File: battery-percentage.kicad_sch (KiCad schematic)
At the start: 12 parts, among them J1 Conn_01x06, SW1 SW_Push, U1 WeMos_D1_mini, U2 LM7805_TO220

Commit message: Updated Schematic
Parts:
- removed D1: LED, LED_THT:LED_D1.8mm_W3.3mm_H2.4mm, symbol Device:LED
- removed R4: 1k, Resistor_THT:R_Axial_DIN0204_L3.6mm_D1.6mm_P5.08mm_Horizontal, symbol Device:R
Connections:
- net +12V: now also C3.2
- net GND: now also C1.2, C3.1; no longer C3.2
- net D1: now reaches U1.14 (SCL/D1)
- net D1: now also J1.2 (Pin_2)
- net D4: no longer names the net of U1.11 (D4)
- net D4: no longer J1.2 (Pin_2)
- no-connect marks 0 -> 9
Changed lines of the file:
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@@
   (junction (at 100.584 80.645) (diameter 0) (color 0 0 0 0)
   )
+  (junction (at 100.584 93.345) (diameter 0) (color 0 0 0 0)
+  )
   (junction (at 105.156 37.211) (diameter 0) (color 0 0 0 0)
   )
@@
   (junction (at 105.156 34.671) (diameter 0) (color 0 0 0 0)
   )
+  (no_connect (at 46.736 59.817))
+  (no_connect (at 46.736 64.897))
+  (no_connect (at 46.736 54.737))
+  (no_connect (at 46.736 44.577))
+  (no_connect (at 26.416 44.577))
+  (no_connect (at 46.736 49.657))
+  (no_connect (at 46.736 62.357))
+  (no_connect (at 46.736 57.277))
+  (no_connect (at 39.116 34.417))
   (wire (pts (xy 112.268 93.345) (xy 112.268 94.615))
     (stroke (width 0) (type default))
@@
     (stroke (width 0) (type default))
   )
-  (wire (pts (xy 110.109 93.345) (xy 112.268 93.345))
-    (stroke (width 0) (type default))
-  )
   (wire (pts (xy 123.952 80.645) (xy 123.952 78.359))
     (stroke (width 0) (type default))
   )
+  (wire (pts (xy 100.584 93.345) (xy 112.268 93.345))
+    (stroke (width 0) (type default))
+  )
   (wire (pts (xy 105.283 37.211) (xy 105.156 37.211))
     (stroke (width 0) (type default))
   )
+  (wire (pts (xy 94.996 93.345) (xy 94.996 90.805))
+    (stroke (width 0) (type default))
+  )
   (wire (pts (xy 123.952 83.185) (xy 123.952 80.645))
     (stroke (width 0) (type default))
   )
-  (wire (pts (xy 155.448 46.355) (xy 155.448 48.895))
-    (stroke (width 0) (type default))
-  )
   (wire (pts (xy 100.584 83.185) (xy 100.584 80.645))
     (stroke (width 0) (type default))
@@
     (stroke (width 0) (type default))
   )
-  (wire (pts (xy 49.276 54.737) (xy 46.736 54.737))
-    (stroke (width 0) (type default))
-  )
   (wire (pts (xy 71.247 33.528) (xy 71.247 35.814))
     (stroke (width 0) (type default))
@@
     (stroke (width 0) (type default))
   )
-  (wire (pts (xy 100.584 93.345) (xy 102.489 93.345))
+  (wire (pts (xy 94.996 93.345) (xy 100.584 93.345))
     (stroke (width 0) (type default))
   )
@@
     (stroke (width 0) (type default))
   )
-  (wire (pts (xy 155.448 36.195) (xy 155.448 38.735))
-    (stroke (width 0) (type default))
-  )
   (wire (pts (xy 112.268 88.265) (xy 112.268 93.345))
     (stroke (width 0) (type default))
   )
-  (wire (pts (xy 155.448 56.515) (xy 155.448 59.055))
-    (stroke (width 0) (type default))
-  )
   (wire (pts (xy 102.743 47.371) (xy 102.743 44.831))
     (stroke (width 0) (type default))
@@
     (stroke (width 0) (type default))
   )
+  (wire (pts (xy 49.276 47.117) (xy 46.736 47.117))
+    (stroke (width 0) (type default))
+  )
   (wire (pts (xy 105.283 47.371) (xy 105.156 47.371))
     (stroke (width 0) (type default))
@@
     (stroke (width 0) (type default))
   )
+  (wire (pts (xy 94.996 83.185) (xy 94.996 80.645))
+    (stroke (width 0) (type default))
+  )
   (wire (pts (xy 105.156 39.751) (xy 102.743 39.751))
     (stroke (width 0) (type default))
   )
   (wire (pts (xy 105.156 34.671) (xy 102.743 34.671))
+    (stroke (width 0) (type default))
+  )
+  (wire (pts (xy 94.996 80.645) (xy 100.584 80.645))
     (stroke (width 0) (type default))
   )
@@
     (effects (font (size 1.27 1.27)) (justify right bottom))
   )
-  (label "D4" (at 49.276 54.737 0) (fields_autoplaced)
-    (effects (font (size 1.27 1.27)) (justify left bottom))
-  )
   (label "FLASH" (at 134.874 43.434 90) (fields_autoplaced)
     (effects (font (size 1.27 1.27)) (justify left bottom))
@@
     (effects (font (size 1.27 1.27)) (justify right bottom))
   )
+  (label "D1" (at 49.276 47.117 0) (fields_autoplaced)
+    (effects (font (size 1.27 1.27)) (justify left bottom))
+  )
   (label "A0" (at 46.736 42.037 0) (fields_autoplaced)
     (effects (font (size 1.27 1.27)) (justify left bottom))
   )
-  (label "D4" (at 102.743 37.211 180) (fields_autoplaced)
+  (label "D1" (at 102.743 37.211 180) (fields_autoplaced)
     (effects (font (size 1.27 1.27)) (justify right bottom))
   )
@@
     )
   )
-  (symbol (lib_id "Device:LED") (at 155.448 42.545 90) (unit 1)
-    (in_bom yes) (on_board yes) (dnp no) (fields_autoplaced)
-    (property "Reference" "D1" (at 158.369 43.4975 90)
-      (effects (font (size 1.27 1.27)) (justify right))
-    )
-    (property "Value" "LED" (at 158.369 46.0375 90)
-      (effects (font (size 1.27 1.27)) (justify right))
-    )
-    (property "Footprint" "LED_THT:LED_D1.8mm_W3.3mm_H2.4mm" (at 155.448 42.545 0)
-      (effects (font (size 1.27 1.27)) hide)
-    )
-    (property "Datasheet" "~" (at 155.448 42.545 0)
-      (effects (font (size 1.27 1.27)) hide)
-    )
-    (pin "1")
-    (pin "2")
-    (instances
-      (project "battery-percentage"
-        (path "/f79966b4-4927-4ec7-886d-17305cb22602"
-          (reference "D1") (unit 1)
-        )
-      )
-    )
-  )
   (symbol (lib_id "power:GND") (at 134.874 58.674 0) (unit 1)
     (in_bom yes) (on_board yes) (dnp no) (fields_autoplaced)
@@
         (path "/f79966b4-4927-4ec7-886d-17305cb22602"
           (reference "#PWR08") (unit 1)
-        )
-      )
-    )
-  )
-  (symbol (lib_id "Device:C") (at 106.299 93.345 90) (unit 1)
-    (in_bom yes) (on_board yes) (dnp no)
-    (property "Reference" "C3" (at 104.14 94.742 90)
-      (effects (font (size 1.27 1.27)) (justify left))
-    )
-    (property "Value" "0.1uF" (at 107.188 96.647 90)
-      (effects (font (size 1.27 1.27)) (justify left))
-    )
-    (property "Footprint" "Capacitor_THT:CP_Radial_D4.0mm_P1.50mm" (at 110.109 92.3798 0)
-      (effects (font (size 1.27 1.27)) hide)
-    )
-    (property "Datasheet" "~" (at 106.299 93.345 0)
-      (effects (font (size 1.27 1.27)) hide)
-    )
-    (pin "1")
-    (pin "2")
-    (instances
-      (project "battery-percentage"
-        (path "/f79966b4-4927-4ec7-886d-17305cb22602"
-          (reference "C3") (unit 1)
         )
       )
@@
     )
   )
-  (symbol (lib_id "power:GND") (at 155.448 59.055 0) (unit 1)
-    (in_bom yes) (on_board yes) (dnp no) (fields_autoplaced)
-    (property "Reference" "#PWR012" (at 155.448 65.405 0)
-      (effects (font (size 1.27 1.27)) hide)
-    )
-    (property "Value" "GND" (at 155.448 63.754 0)
-      (effects (font (size 1.27 1.27)))
-    )
-    (property "Footprint" "" (at 155.448 59.055 0)
-      (effects (font (size 1.27 1.27)) hide)
-    )
-    (property "Datasheet" "" (at 155.448 59.055 0)
-      (effects (font (size 1.27 1.27)) hide)
-    )
-    (pin "1")
-    (instances
-      (project "battery-percentage"
-        (path "/f79966b4-4927-4ec7-886d-17305cb22602"
-          (reference "#PWR012") (unit 1)
-        )
-      )
-    )
-  )
   (symbol (lib_id "power:+5V") (at 123.952 78.359 0) (unit 1)
     (in_bom yes) (on_board yes) (dnp no) (fields_autoplaced)
@@
   (symbol (lib_id "Device:C") (at 100.584 86.995 0) (unit 1)
     (in_bom yes) (on_board yes) (dnp no)
-    (property "Reference" "C1" (at 93.472 85.979 0)
-      (effects (font (size 1.27 1.27)) (justify left))
-    )
-    (property "Value" "0.2uF" (at 91.821 87.884 0)
+    (property "Reference" "C1" (at 104.902 86.106 0)
+      (effects (font (size 1.27 1.27)) (justify left))
+    )
+    (property "Value" "0.2uF" (at 103.251 88.011 0)
       (effects (font (size 1.27 1.27)) (justify left))
     )
@@
     )
   )
-  (symbol (lib_id "power:+5V") (at 155.448 36.195 0) (unit 1)
-    (in_bom yes) (on_board yes) (dnp no) (fields_autoplaced)
-    (property "Reference" "#PWR011" (at 155.448 40.005 0)
-      (effects (font (size 1.27 1.27)) hide)
-    )
-    (property "Value" "+5V" (at 155.448 32.639 0)
-      (effects (font (size 1.27 1.27)))
-    )
-    (property "Footprint" "" (at 155.448 36.195 0)
-      (effects (font (size 1.27 1.27)) hide)
-    )
-    (property "Datasheet" "" (at 155.448 36.195 0)
-      (effects (font (size 1.27 1.27)) hide)
-    )
-    (pin "1")
-    (instances
-      (project "battery-percentage"
-        (path "/f79966b4-4927-4ec7-886d-17305cb22602"
-          (reference "#PWR011") (unit 1)
-        )
-      )
-    )
-  )
   (symbol (lib_id "Device:R") (at 71.247 39.624 0) (unit 1)
     (in_bom yes) (on_board yes) (dnp no) (fields_autoplaced)
@@
         (path "/f79966b4-4927-4ec7-886d-17305cb22602"
           (reference "#PWR03") (unit 1)
-        )
-      )
-    )
-  )
-  (symbol (lib_id "Device:R") (at 155.448 52.705 0) (unit 1)
-    (in_bom yes) (on_board yes) (dnp no) (fields_autoplaced)
-    (property "Reference" "R4" (at 158.369 52.07 0)
-      (effects (font (size 1.27 1.27)) (justify left))
-    )
-    (property "Value" "1k" (at 158.369 54.61 0)
-      (effects (font (size 1.27 1.27)) (justify left))
-    )
-    (property "Footprint" "Resistor_THT:R_Axial_DIN0204_L3.6mm_D1.6mm_P5.08mm_Horizontal" (at 153.67 52.705 90)
-      (effects (font (size 1.27 1.27)) hide)
-    )
-    (property "Datasheet" "~" (at 155.448 52.705 0)
-      (effects (font (size 1.27 1.27)) hide)
-    )
-    (pin "1")
-    (pin "2")
-    (instances
-      (project "battery-percentage"
-        (path "/f79966b4-4927-4ec7-886d-17305cb22602"
-          (reference "R4") (unit 1)
         )
       )
@@
         )
       )
+    )
+  )
+  (symbol (lib_id "Device:C") (at 94.996 86.995 180) (unit 1)
+    (in_bom yes) (on_board yes) (dnp no)
+    (property "Reference" "C3" (at 91.313 88.265 0)
+      (effects (font (size 1.27 1.27)) (justify left))
+    )
+    (property "Value" "0.1uF" (at 92.075 86.233 0)
+      (effects (font (size 1.27 1.27)) (justify left))
+    )
+    (property "Footprint" "Capacitor_THT:CP_Radial_D4.0mm_P1.50mm" (at 94.0308 83.185 0)
+      (effects (font (size 1.27 1.27)) hide)
+    )
+    (property "Datasheet" "~" (at 94.996 86.995 0)
+      (effects (font (size 1.27 1.27)) hide)
+    )
+    (pin "1")
+    (pin "2")
+    (instances
+      (project "battery-percentage"
+        (path "/f79966b4-4927-4ec7-886d-17305cb22602"
+          (reference "C3") (unit 1)
+        )
+      )

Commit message: Updated Schematic
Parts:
- removed J1: Conn_01x06, Connector_PinHeader_2.00mm:PinHeader_1x06_P2.00mm_Horizontal, symbol Connector_Generic:Conn_01x06
- added J2: Conn_01x07, symbol Connector_Generic:Conn_01x07
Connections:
- net +12V: now also J2.1 (Pin_1)
- net +5V: now also J2.5 (Pin_5)
- net D1: now also J2.2 (Pin_2)
- net GND: now also J2.6 (Pin_6), J2.7 (Pin_7)
- net RX: now also J2.3 (Pin_3)
- net TX: now also J2.4 (Pin_4)

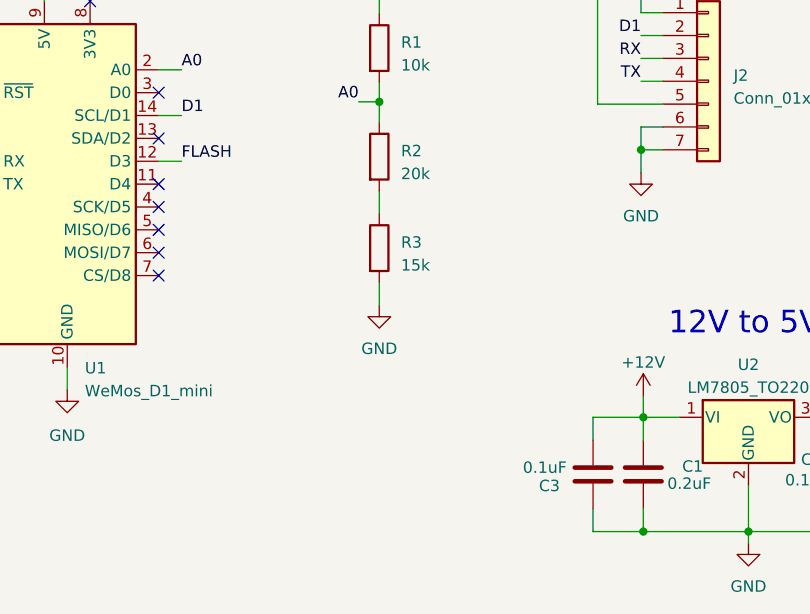
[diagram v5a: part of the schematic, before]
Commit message: Updated Potential Divider Values
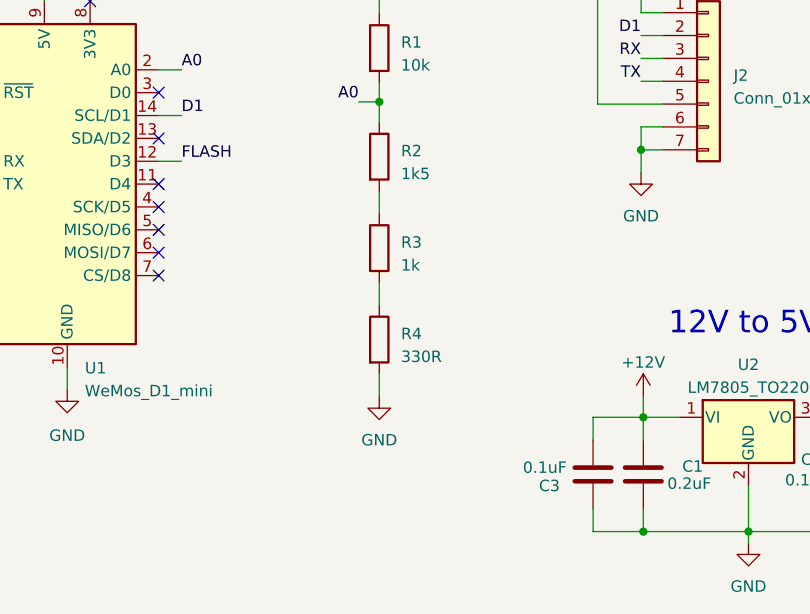
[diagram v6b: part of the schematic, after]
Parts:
- added R4: 330R, Resistor_THT:R_Axial_DIN0204_L3.6mm_D1.6mm_P5.08mm_Horizontal, symbol Device:R
- R2: value 20k -> 1k5
- R3: value 15k -> 1k
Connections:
- net GND: now also R4.2; no longer R3.2
- new net: R3.2, R4.1
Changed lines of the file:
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@@
-    (stroke (width 0) (type default))
-  )
-  (wire (pts (xy 71.247 68.199) (xy 71.247 65.659))
     (stroke (width 0) (type default))
   )
@@
     (stroke (width 0) (type default))
   )
+  (wire (pts (xy 71.247 65.659) (xy 71.247 68.199))
+    (stroke (width 0) (type default))
+  )
   (wire (pts (xy 100.33 35.687) (xy 102.743 35.687))
     (stroke (width 0) (type default))
@@
   )
   (wire (pts (xy 49.276 42.037) (xy 46.736 42.037))
+    (stroke (width 0) (type default))
+  )
+  (wire (pts (xy 71.247 78.359) (xy 71.247 75.819))
     (stroke (width 0) (type default))
   )
@@
     )
   )
-  (symbol (lib_id "power:GND") (at 71.247 68.199 0) (unit 1)
-    (in_bom yes) (on_board yes) (dnp no) (fields_autoplaced)
-    (property "Reference" "#PWR05" (at 71.247 74.549 0)
-      (effects (font (size 1.27 1.27)) hide)
-    )
-    (property "Value" "GND" (at 71.247 73.025 0)
-      (effects (font (size 1.27 1.27)))
-    )
-    (property "Footprint" "" (at 71.247 68.199 0)
-      (effects (font (size 1.27 1.27)) hide)
-    )
-    (property "Datasheet" "" (at 71.247 68.199 0)
-      (effects (font (size 1.27 1.27)) hide)
-    )
-    (pin "1")
-    (instances
-      (project "battery-percentage"
-        (path "/f79966b4-4927-4ec7-886d-17305cb22602"
-          (reference "#PWR05") (unit 1)
-        )
-      )
-    )
-  )
   (symbol (lib_id "Device:R") (at 71.247 51.689 0) (unit 1)
     (in_bom yes) (on_board yes) (dnp no) (fields_autoplaced)
@@
       (effects (font (size 1.27 1.27)) (justify left))
     )
-    (property "Value" "20k" (at 73.66 53.594 0)
+    (property "Value" "1k5" (at 73.66 53.594 0)
       (effects (font (size 1.27 1.27)) (justify left))
     )
@@
       (effects (font (size 1.27 1.27)) (justify left))
     )
-    (property "Value" "15k" (at 73.66 63.754 0)
+    (property "Value" "1k" (at 73.66 63.754 0)
       (effects (font (size 1.27 1.27)) (justify left))
     )
@@
     )
   )
+  (symbol (lib_id "power:GND") (at 71.247 78.359 0) (unit 1)
+    (in_bom yes) (on_board yes) (dnp no) (fields_autoplaced)
+    (property "Reference" "#PWR05" (at 71.247 84.709 0)
+      (effects (font (size 1.27 1.27)) hide)
+    )
+    (property "Value" "GND" (at 71.247 83.185 0)
+      (effects (font (size 1.27 1.27)))
+    )
+    (property "Footprint" "" (at 71.247 78.359 0)
+      (effects (font (size 1.27 1.27)) hide)
+    )
+    (property "Datasheet" "" (at 71.247 78.359 0)
+      (effects (font (size 1.27 1.27)) hide)
+    )
+    (pin "1")
+    (instances
+      (project "battery-percentage"
+        (path "/f79966b4-4927-4ec7-886d-17305cb22602"
+          (reference "#PWR05") (unit 1)
+        )
+      )
+    )
+  )
   (symbol (lib_id "power:+5V") (at 123.952 78.359 0) (unit 1)
     (in_bom yes) (on_board yes) (dnp no) (fields_autoplaced)
@@
         )
       )
+    )
+  )
+  (symbol (lib_id "Device:R") (at 71.247 72.009 0) (unit 1)
+    (in_bom yes) (on_board yes) (dnp no) (fields_autoplaced)
+    (property "Reference" "R4" (at 73.66 71.374 0)
+      (effects (font (size 1.27 1.27)) (justify left))
+    )
+    (property "Value" "330R" (at 73.66 73.914 0)
+      (effects (font (size 1.27 1.27)) (justify left))
+    )
+    (property "Footprint" "Resistor_THT:R_Axial_DIN0204_L3.6mm_D1.6mm_P5.08mm_Horizontal" (at 69.469 72.009 90)
+      (effects (font (size 1.27 1.27)) hide)
+    )
+    (property "Datasheet" "~" (at 71.247 72.009 0)
+      (effects (font (size 1.27 1.27)) hide)
+    )
+    (pin "1")
+    (pin "2")
+    (instances
+      (project "battery-percentage"
+        (path "/f79966b4-4927-4ec7-886d-17305cb22602"
+          (reference "R4") (unit 1)
+        )
+      )

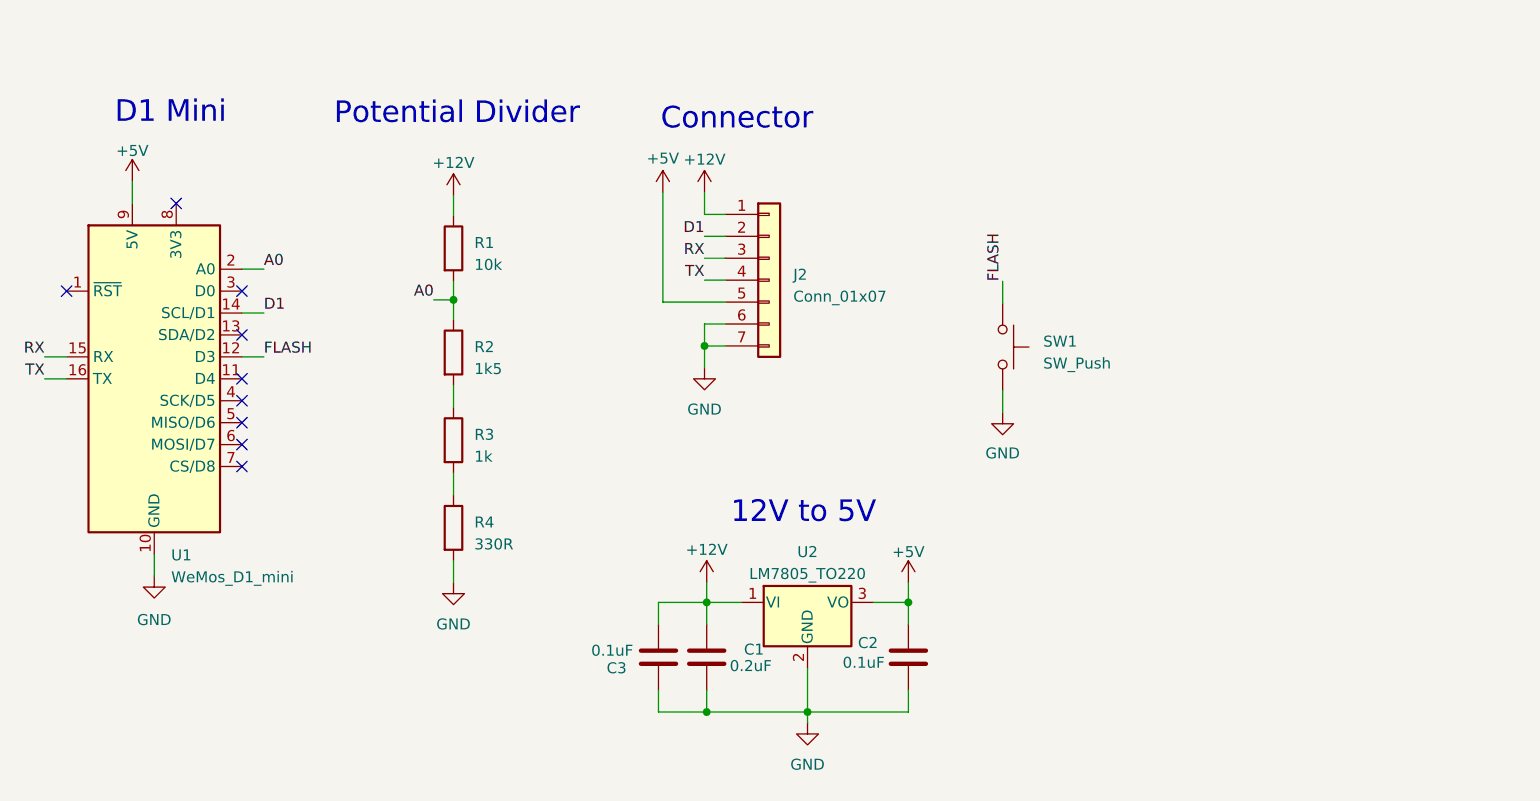
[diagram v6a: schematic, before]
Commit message: Added CAN BUS Connector Socket
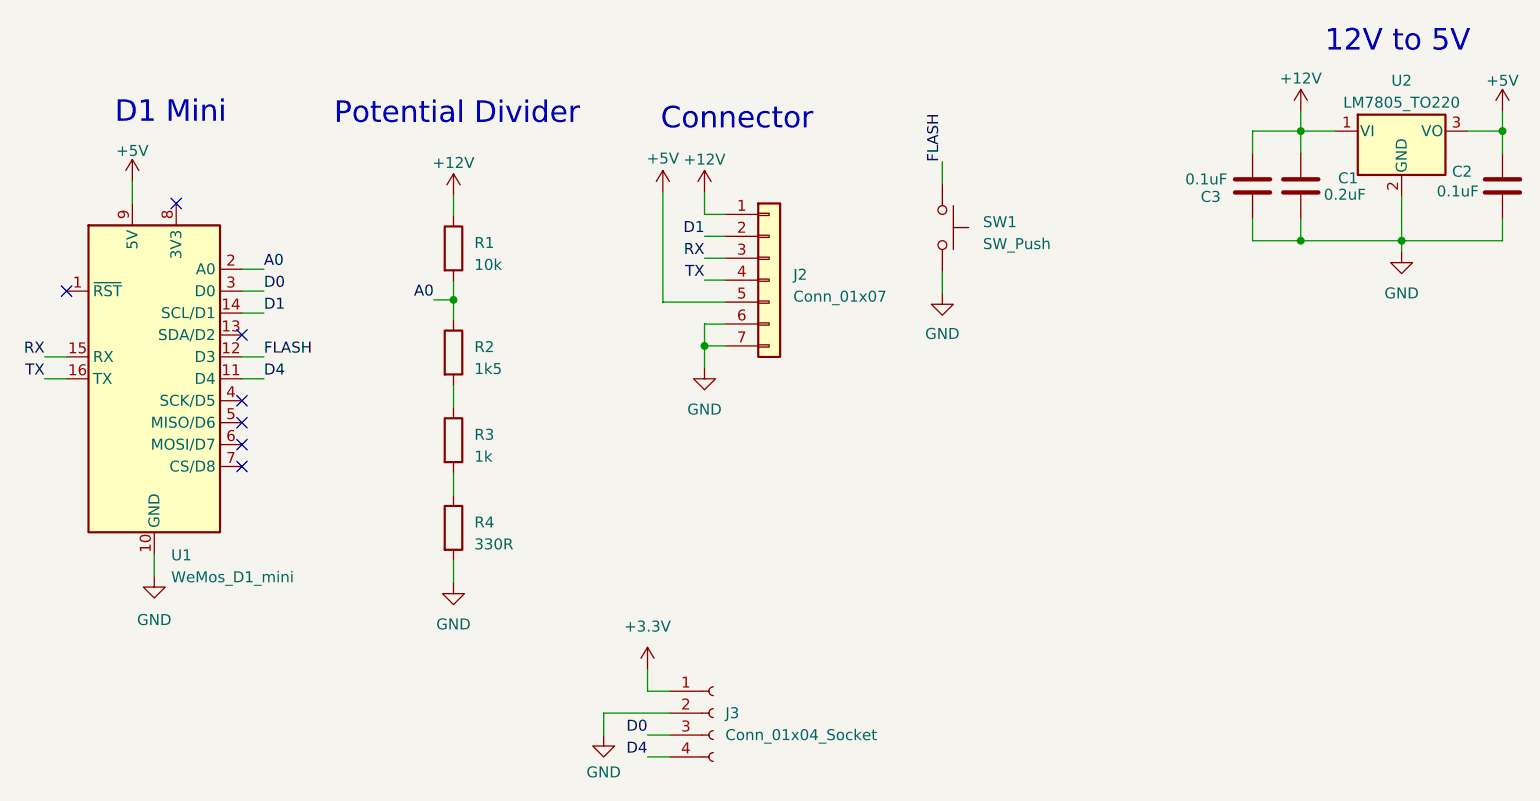
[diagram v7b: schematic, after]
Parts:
- added J3: Conn_01x04_Socket, symbol Connector:Conn_01x04_Socket
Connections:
- net GND: now also J3.2 (Pin_2)
- net D4: now reaches U1.11 (D4)
- net D4: now also J3.4 (Pin_4)
- net D0: now reaches U1.3 (D0)
- net D0: now also J3.3 (Pin_3)
- new net +3.3V: J3.1 (Pin_1)
- no-connect marks 9 -> 7
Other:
- moved on the sheet: C1, C2, C3, SW1, U2
